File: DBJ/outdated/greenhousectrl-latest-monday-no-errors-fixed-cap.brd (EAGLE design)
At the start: 73.6 x 69.5 mm, 56 parts, among them IC1 ATMEGA168TQFP-08, IC2 7824DT, IC4 L298, J1 POWER_JACKPTH, K2 G5LE, Q1 MMBT2222A, SW2 MOMENTARYBUTTON, X1 CRYSTALS-NOGND-HC49

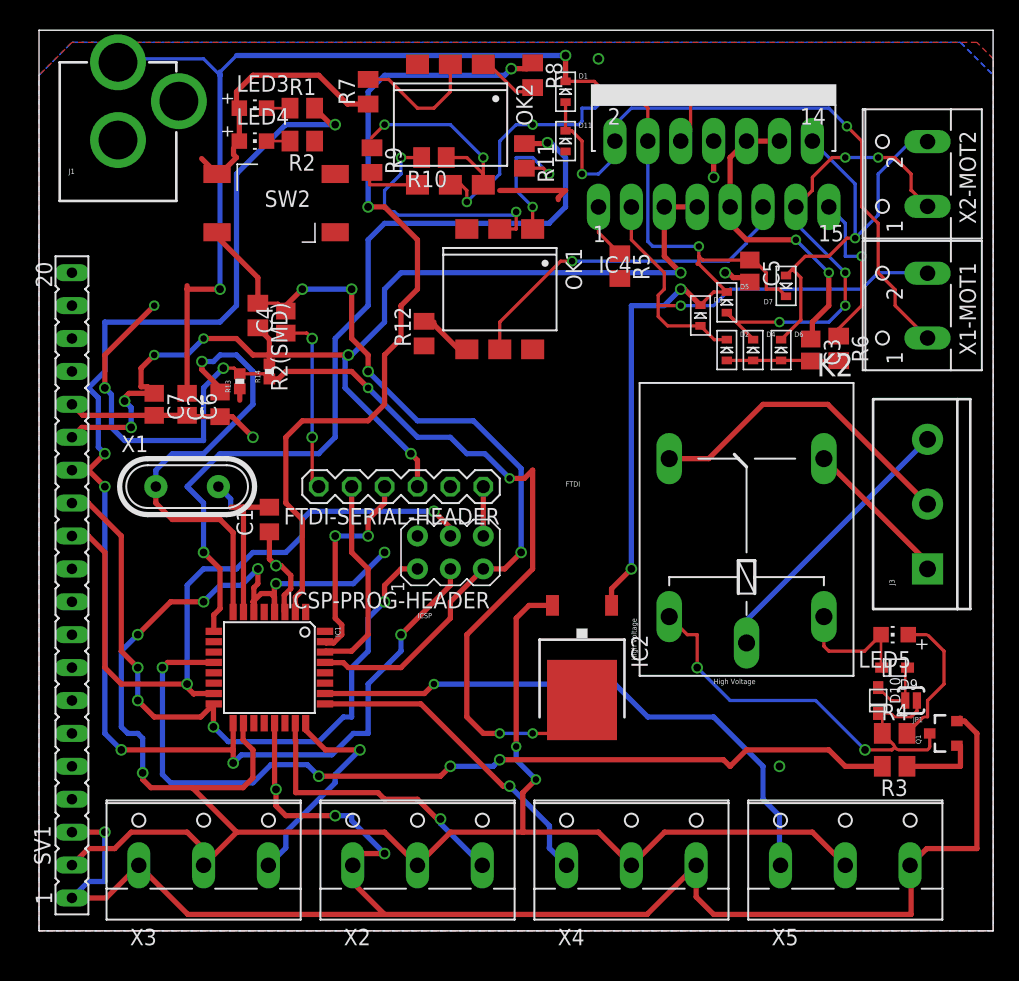
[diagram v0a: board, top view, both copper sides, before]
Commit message: Replaced 1x20 LCD with 2 1x8, gerb and DRC checked
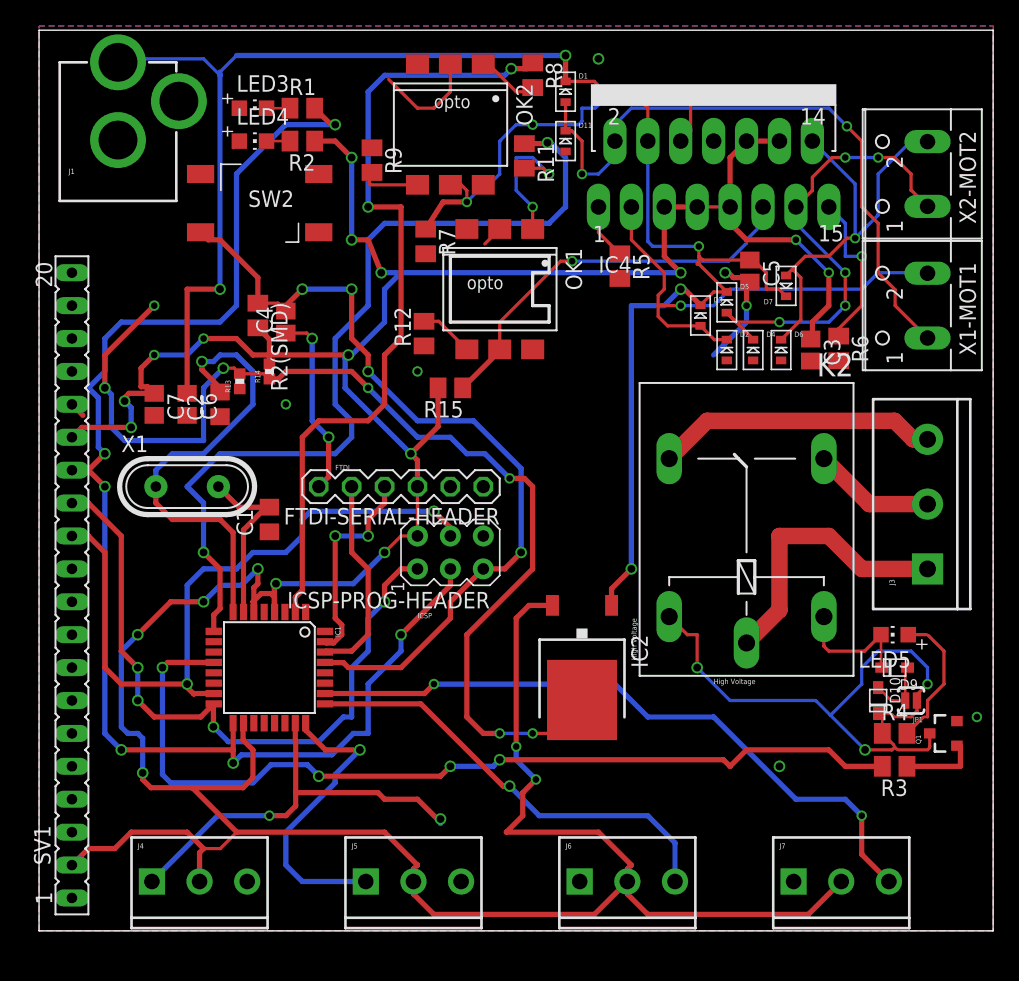
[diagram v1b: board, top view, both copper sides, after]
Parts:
- removed R10: (no value), adafruit:M0805
- removed X2, X3, X4, X5: (no value), ece388:W237-103
- added J4, J5, J6, J7: (no value), SparkFun-Connectors:SCREWTERMINAL-3.5MM-3_LOCK.007S
- added R15: 1k, adafruit:M0805
- C1, C2: value (none) -> 20pF
- R1, R2: value (none) -> 150
- R11, R8: value (none) -> 240
- R12, R14, R7, R9: value (none) -> 1k
- R13: value (none) -> 3k
- R2(SMD), R5, R6: value (none) -> 10k
- R4: value 1K -> 150
- moved R7 12.4 mm to (29.8, 53.2), turned to 270 degrees
- moved SW2 1.27 mm to (21.6, 58.4)
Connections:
- removed net N$4: OK2.2, R7.2
- removed net N$9: OK1.2, R10.2
- net +5V: now also J4.2, J5.2, J6.2, J7.2, R15.2, R7.2; no longer X2.2, X3.2, X4.2, X5.2
- net COMMON: now also J3.1; no longer J3.3
- net ENA: now also R7.1
- net ENB: now also R15.1
- net GND: now also J4.3, J5.3, J6.1, J7.1, OK1.2, OK2.2; no longer R10.1, R7.1, X2.1, X3.1, X4.3, X5.3
- net NC: now also J3.2; no longer J3.1
- net NO: now also J3.3; no longer J3.2
- net PC0: now also J4.1; no longer X2.3
- net PC1: now also J5.1; no longer X3.3
- net PC2: now also J6.3; no longer X4.1
- net PC3: now also J7.3; no longer X5.1
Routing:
- net GND: track 209.5 -> 21.2 mm, vias 10 -> 5
- net +5V: track 259.3 -> 306.0 mm, vias 17 -> 20
- net N$9: track 19.5 -> 0.00 mm, vias 2 -> 0
- net COIL: track 34.0 -> 47.7 mm, vias 2 -> 3
- net PC0: track 22.3 -> 32.3 mm, vias 1 -> 2
- net N$4: track 9.90 -> 0.00 mm
- net PC2: track 24.9 -> 34.4 mm
- net PC3: track 44.9 -> 51.9 mm, vias 1 -> 2
- net PC1: track 17.2 -> 23.3 mm
- net ENA: track 29.3 -> 33.7 mm
- net ENB: track 27.0 -> 31.2 mm
- net NO: track 24.9 -> 21.7 mm
- net NC: track 11.8 -> 9.45 mm
- net PD4: track 64.5 -> 62.4 mm
- net PD5: track 65.5 -> 67.3 mm
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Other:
- board text added: "opto"
